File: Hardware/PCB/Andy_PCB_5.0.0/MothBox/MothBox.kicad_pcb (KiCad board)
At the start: 2 copper layers, 237 x 140.5 mm, 184 parts, among them P1 Raw Input, P2 12V Regulated Input, P3 Input to regulator, P4 External Attractor, Q1 BC817, Q10 BC817, Q11 BC817, Q2 TJ10S04M3L,LXHQ, Q4 BC817, Q5 TJ10S04M3L,LXHQ, Q6 BC817, Q7 TJ10S04M3L,LXHQ, Q8 BC817, Q9 BC817, U1 Days, U10 IRF9335TRPBF, U11 IRF9335TRPBF, U12 IRF9335TRPBF, U13 IRF9335TRPBF, U16 Female Inv Socket Pi 2.54-2*20, U18 RASPBERRY_PI_4B_4GB, U19 INA219BIDCNT, U2 Hours1, U3 XL4015E1, U5 RASPBERRY_PI_5, U6 Hours2, U7 Modes, U8 CD74HC4067M96E4, U9 CD74HC4067M96E4

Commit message: fillet lines
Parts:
- removed D1: S10MC, easyeda2kicad:SMC_L7.1-W6.2-LS8.1-RD
- added H9: GPS 4 pin 2.54-1*4P母, AQLibrary:GPS4pin_HDR-TH_4P-P2.54-V-F, F.Cu at (-46.5, 49.5)
- added U17: GPs 5 pin PM2.54-1*5, AQLibrary:GPS5pin_HDR-TH_5P-P2.54-V-F, F.Cu at (-18.6, 48.5)
- R64, R65: value 10K -> 4k7
- U5: footprint Connector_PinHeader_2.54mm:PinHeader_2x20_P2.54mm_Vertical -> AQLibrary:EPAPER_PinHeader_2x20_P2.54mm_Vertical
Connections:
- net /RPI5/STM_RX renamed GPS_TX
- net /RPI5/STM_TX renamed GPS_RX
- F2 pad 2: Net-(F2-Pad2) -> /Power/PWR_IN
- P1 pad 2: Net-(F2-Pad2) -> /Power/PWR_IN
- P2 pad 2: Net-(D1-A) -> +12V
- P3 pad 2: /Power/PWR_IN -> /Power/VIN-
- Q2 pad 3: /Power/PWR_IN -> /Power/VIN-
- R1 pad 2: /Power/PWR_IN -> /Power/VIN-
- R63 pad 1: /Power/PWR_IN -> /Power/VIN-
- U19 pad 2: /Power/PWR_IN -> /Power/VIN-
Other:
- outline, holes or cut-outs redrawn

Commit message: Tweaked Mothbeam and added GPS footprints
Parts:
- removed H4, H7: MountingHole_1/4inbolt, MountingHole:MountingHole_6.4mm_M6_Pad
- removed JP1: SolderJumper_2_Open, Jumper:SolderJumper-2_P1.3mm_Open_RoundedPad1.0x1.5mm
- A1, A2, A3: footprint Attractor:attractor -> Attractor:HDR-TH_4P-P2.54-H-M-W10.4
- E3: footprint SK54C:DIO_SK54C -> easyeda2kicad:SMC_L6.9-W5.9-LS8.0-RD
- H9, U17: moved to B.Cu
- P1, P2, P3, P4: footprint easyeda2kicad:CONN-TH_DB301V-3.5-2P-GN -> easyeda2kicad:CONN-TH_2P-P5.08_DIBO_DB142R-5.08-2P
- moved P4 160.3 mm to (102.5, 117.8), turned to -90 degrees
- moved R58 153.7 mm to (181.5, 81.8), turned to -90 degrees
- moved R55 141.7 mm to (178.5, 81.8)
- moved R48 128.4 mm to (191.2, 84.8)
- moved R47 128.4 mm to (193.5, 84.8)
- moved H9 121.1 mm to (53.2, 118.2), turned to -90 degrees
- moved R50 115.5 mm to (185.3, 81.8)
- moved R49 115.5 mm to (187.5, 81.8)
- moved U17 106.9 mm to (62.5, 118.2), turned to -90 degrees
- moved A1 99.1 mm to (196.5, 71.8), turned to -90 degrees
- moved U13 89.8 mm to (149.5, 89.8)
- moved L1 67.1 mm to (166.5, 105.8)
- moved U12 62.2 mm to (154.5, 75.8)
- moved A3 52.8 mm to (102.5, 71.8), turned to -90 degrees
- moved A2 31.9 mm to (249.5, 71.8), turned to -90 degrees
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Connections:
- net /Switches/Armed/Disarmed renamed /GPS and Switches/Armed/Disarmed
- net /Switches/Attractor_1 renamed /GPS and Switches/Attractor_1
- net /Switches/Attractor_2 renamed /GPS and Switches/Attractor_2
- net /Switches/Attractor_3 renamed /GPS and Switches/Attractor_3
- net /Switches/C1 renamed /GPS and Switches/C1
- net /Switches/C2 renamed /GPS and Switches/C2
- net /Switches/Fri renamed /GPS and Switches/Fri
- net /Switches/HI/LOW_PWR renamed /GPS and Switches/HI/LOW_PWR
- net /Switches/Hour_1 renamed /GPS and Switches/Hour_1
- net /Switches/Hour_10 renamed /GPS and Switches/Hour_10
- net /Switches/Hour_11 renamed /GPS and Switches/Hour_11
- net /Switches/Hour_12 renamed /GPS and Switches/Hour_12
- net /Switches/Hour_13 renamed /GPS and Switches/Hour_13
- net /Switches/Hour_14 renamed /GPS and Switches/Hour_14
- net /Switches/Hour_15 renamed /GPS and Switches/Hour_15
- net /Switches/Hour_16 renamed /GPS and Switches/Hour_16
- net /Switches/Hour_2 renamed /GPS and Switches/Hour_2
- net /Switches/Hour_3 renamed /GPS and Switches/Hour_3
- net /Switches/Hour_4 renamed /GPS and Switches/Hour_4
- net /Switches/Hour_5 renamed /GPS and Switches/Hour_5
- net /Switches/Hour_6 renamed /GPS and Switches/Hour_6
- net /Switches/Hour_7 renamed /GPS and Switches/Hour_7
- net /Switches/Hour_8 renamed /GPS and Switches/Hour_8
- net /Switches/Hour_9 renamed /GPS and Switches/Hour_9
- net /Switches/INT/EXT_Attractor renamed /GPS and Switches/INT/EXT_Attractor
- net /Switches/Mon renamed /GPS and Switches/Mon
- net /Switches/Sat renamed /GPS and Switches/Sat
- net /Switches/Sun renamed /GPS and Switches/Sun
- net /Switches/Test_Debug renamed /GPS and Switches/Test_Debug
- net /Switches/Thur renamed /GPS and Switches/Thur
- net /Switches/Tue renamed /GPS and Switches/Tue
- net /Switches/Wed renamed /GPS and Switches/Wed
- A1 pad 1: unconnected-(A1-EN-Pad1) -> /UV LED PCB/+12V_PCB2
- A1 pad 2: unconnected-(A1-EN-Pad2) -> /UV LED PCB/+12V_PCB2
- A1 pad 3: /UV LED PCB/+12V_PCB2 -> GND
- A1 pad 4: /UV LED PCB/+12V_PCB2 -> GND
- A2 pad 1: unconnected-(A2-EN-Pad1) -> /UV LED PCB/+12V_PCB1
- A2 pad 2: unconnected-(A2-EN-Pad2) -> /UV LED PCB/+12V_PCB1
- A2 pad 3: /UV LED PCB/+12V_PCB1 -> GND
- A2 pad 4: /UV LED PCB/+12V_PCB1 -> GND
- A3 pad 1: unconnected-(A3-EN-Pad1) -> /UV LED PCB/+12V_PCB3
- A3 pad 2: unconnected-(A3-EN-Pad2) -> /UV LED PCB/+12V_PCB3
- A3 pad 3: /UV LED PCB/+12V_PCB3 -> GND
- A3 pad 4: /UV LED PCB/+12V_PCB3 -> GND
- L1 pad 1: Net-(E3-PadC) -> Net-(E3-C)
- U16 pad 30: EN_MUX2 -> EN_MUX1
- U16 pad 31: /RPI5/TimeP -> GPS_PPS
- U16 pad 32: L_LED_CTRL -> EN_MUX2
- U16 pad 36: RPI_CTRL -> L_LED_CTRL
- U3 pad 3: Net-(E3-PadC) -> Net-(E3-C)
- U5 pad 29: EN_MUX2 -> EN_MUX1
- U5 pad 31: L_LED_CTRL -> EN_MUX2
- U5 pad 32: /RPI5/TimeP -> GPS_PPS
- U5 pad 35: RPI_CTRL -> L_LED_CTRL
- U8 pad 15: GND -> EN_MUX1
- U9 pad 15: GND -> EN_MUX2
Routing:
- net GND: vias 143 -> 131
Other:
- board text added: "+ -"
- board text added: "Regulator Input"
- board text removed: "DAYS"
- board text removed: "HI UV INT LO FUL EX"
- board text removed: "LED LEVEL"
- board text removed: "to Regulator"

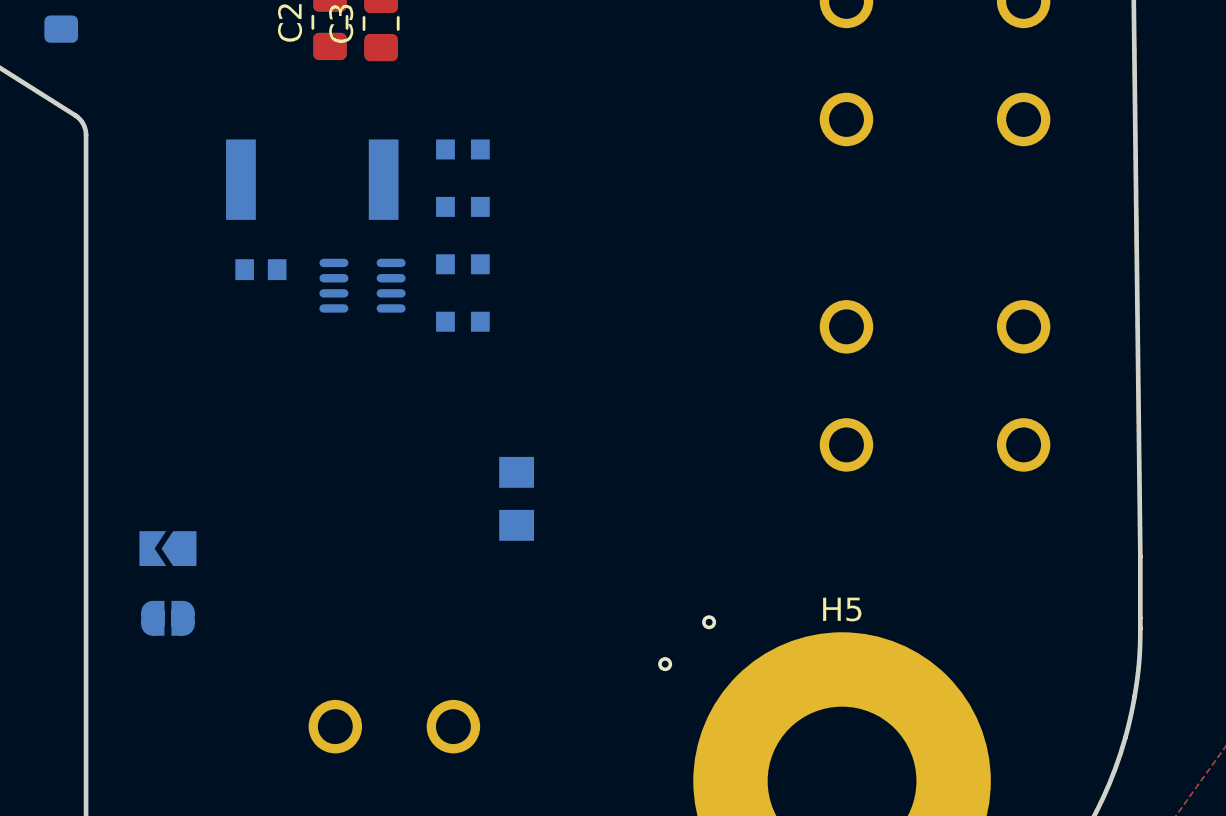
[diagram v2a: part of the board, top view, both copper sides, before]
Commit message: started adding test points, fixed current sensor should be 3.3v
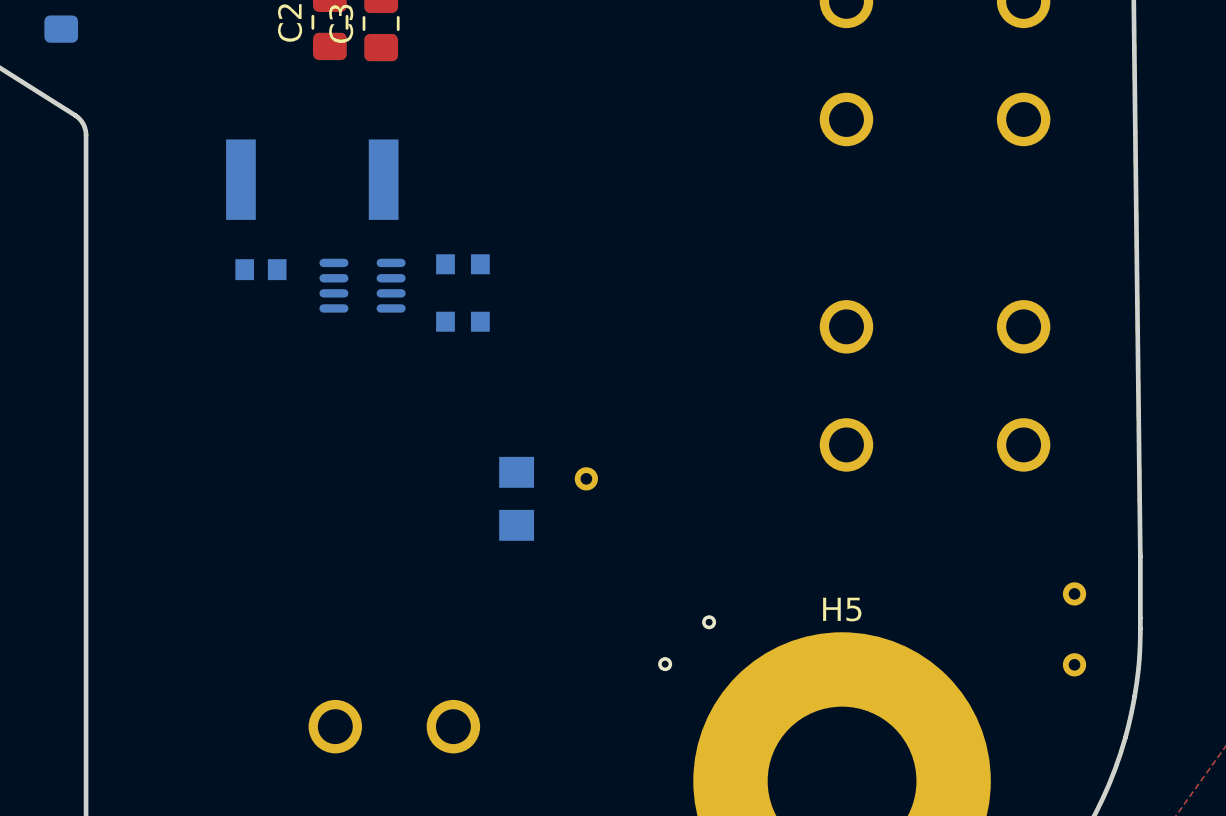
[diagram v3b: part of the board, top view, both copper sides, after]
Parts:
- removed R61, R62: 10K, easyeda2kicad:R0603
- removed SJ1: SOLDERJUMPERREFLOW_NOPASTE, Jumper:SolderJumper-2_P1.3mm_Open_RoundedPad1.0x1.5mm
- removed SJ2: SOLDERJUMPERREFLOW_NOPASTE, Jumper:SolderJumper-2_P1.3mm_Open_TrianglePad1.0x1.5mm
- added TP1: TestPoint, TestPoint:TestPoint_THTPad_D1.0mm_Drill0.5mm, B.Cu at (265.5, 184.7)
- added TP2: TestPoint, TestPoint:TestPoint_THTPad_D1.0mm_Drill0.5mm, B.Cu at (265.5, 187.8)
- added TP3: TestPoint, TestPoint:TestPoint_THTPad_D1.0mm_Drill0.5mm, B.Cu at (244.5, 179.8)
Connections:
- C6 pad 2: +5V -> +3.3V
- R64 pad 2: +5V -> +3.3V
- R65 pad 2: +5V -> +3.3V
- U19 pad 4: +5V -> +3.3V

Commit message: before i kill the pullup resistors
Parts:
- removed R21, R23, R25, R26, R39, R42, R43, R44: DNP, Resistor_SMD:R_0805_2012Metric
- added TP4: VIN_-, TestPoint:TestPoint_THTPad_D1.0mm_Drill0.5mm, B.Cu at (247.5, 175.8)
- C2, C3, R4, R45, R46, R5, R56, R58, R59: moved to B.Cu
- Q10, R2, R3, R79, R81, U10: moved to F.Cu
- R64, R65: value 4k7 -> 10k
- TP1: value TestPoint -> A0_meas
- TP2: value TestPoint -> A1_meas
- TP3: value TestPoint -> 5V_test
- moved R38 382.3 mm to (354.6, 74.3), turned to 90 degrees
- moved R37 377.8 mm to (349.6, 74.3), turned to 90 degrees
- moved R36 373.3 mm to (344.6, 74.3), turned to 90 degrees
- moved R41 362.8 mm to (332.5, 74.3), turned to 90 degrees
- moved R40 358.6 mm to (327.4, 74.3), turned to 90 degrees
- moved R35 352.4 mm to (319.9, 74.3), turned to 90 degrees
- moved R34 348.6 mm to (315.0, 74.3), turned to 90 degrees
- moved R56 341.6 mm to (311.9, 74.3), turned to 90 degrees
- moved R45 297.6 mm to (311.0, 89.8), turned to -90 degrees
- moved R46 294.0 mm to (308.0, 89.8), turned to -90 degrees
- moved R59 209.9 mm to (293.0, 89.8), turned to -90 degrees
- moved R2 184.5 mm to (98.0, 154.8), turned to 0 degrees
- moved R3 176.6 mm to (106.0, 161.3), turned to 0 degrees
- moved R57 149.9 mm to (304.5, 46.8)
- moved U10 129.6 mm to (293.5, 46.3), turned to 0 degrees
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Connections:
- P3 pad 2: /Power/VIN- -> Net-(Q2-D)
- TP3 pad 1: /Power/VIN+ -> +5V
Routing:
- net +3.3V: track 29.0 -> 0.00 mm
- net Net-(Q11-C): track 2.62 -> 0.00 mm
- net +5V: track 0.00 -> 2.54 mm
- net GND: track 2.53 -> 0.00 mm, vias 131 -> 0
- net Net-(Q11-B): track 2.28 -> 0.00 mm
- net Net-(Q9-B): track 2.24 -> 0.00 mm
- net /Power/FB: track 2.15 -> 0.00 mm

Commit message: Groups photos leds, started routing
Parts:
- removed R16, R17, R18, R19, R20, R22, R24, R27, R28, R29, R30, R31, R32, R33, R34, R35, R36, R37, R38, R40, R41, R45, R46, R47, R48, R49, R50, R56, R58, R59, R60: 10k, Resistor_SMD:R_0805_2012Metric
- C17: moved to B.Cu
- D30, D31, Q11, Q8, Q9, R75, R76, R77, R78, R80, R82, U11, U12: moved to F.Cu
- moved R52 547.7 mm to (-208.1, 247.1)
- moved Q7 485.4 mm to (-136.2, 242.8)
- moved R51 445.3 mm to (-313.5, 135.3), turned to 0 degrees
- moved LED20 437.4 mm to (-362.5, 248.2), turned to 180 degrees
- moved LED22 437.2 mm to (-362.5, 255.3), turned to 180 degrees
- moved LED21 436.8 mm to (-362.0, 251.8)
- moved Q5 433.4 mm to (-122.7, 101.8)
- moved R57 433.4 mm to (-123.6, 114.0)
- moved LED25 428.6 mm to (-344.0, 255.3), turned to 180 degrees
- moved R69 421.5 mm to (-129.7, 271.3)
- moved LED24 421.1 mm to (-348.5, 249.8), turned to 90 degrees
- moved LED23 417.0 mm to (-344.5, 244.8)
- moved R66 407.8 mm to (-171.7, 252.8), turned to -90 degrees
- moved LED26 400.0 mm to (-318.0, 244.2)
- moved LED27 400.0 mm to (-318.0, 248.2)
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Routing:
- net /RPI5/GPIO4/GPIO_GCKL: track 0.00 -> 245.4 mm
- net SDA: track 0.00 -> 236.8 mm
- net /RPI5/Save for eink_11: track 0.00 -> 235.4 mm
- net SCL: track 0.00 -> 234.6 mm
- net /RPI5/Save for eink_22: track 0.00 -> 215.6 mm
- net /RPI5/Save for eink_24: track 0.00 -> 209.0 mm
- net /RPI5/Save for eink_19: track 0.00 -> 188.2 mm
- net /RPI5/Save for eink_23: track 0.00 -> 181.0 mm
- net /RPI5/ID_SD: track 0.00 -> 173.8 mm
- net /RPI5/Save for relay: track 0.00 -> 172.8 mm
- net /RPI5/Save for relay 2: track 0.00 -> 164.1 mm
- net L_LED_CTRL: track 0.00 -> 164.0 mm
- net /RPI5/Save for relay 3: track 0.00 -> 161.6 mm
- net GPS_TX: track 0.00 -> 60.3 mm
- net +3.3V: track 0.00 -> 37.6 mm
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- removed copper zone on B.Cu, net +12V

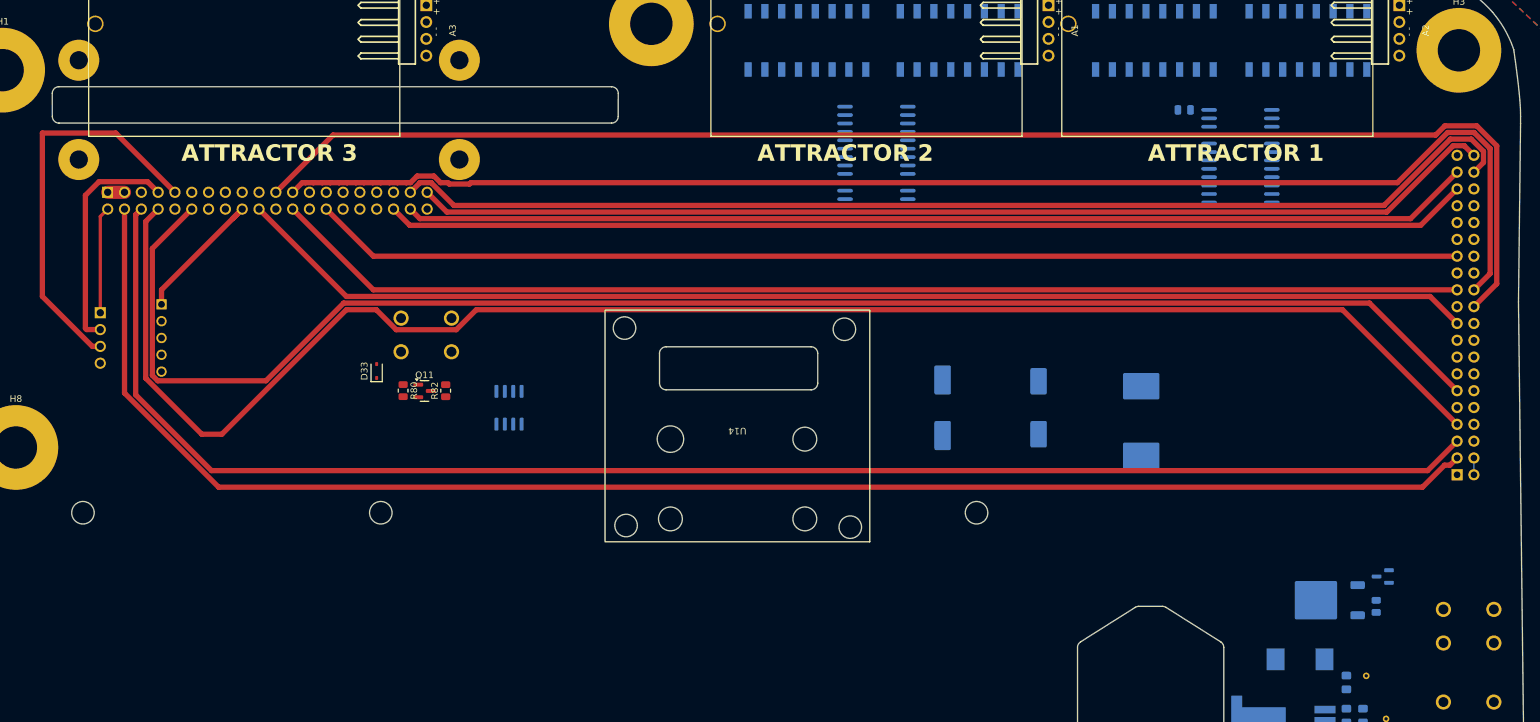
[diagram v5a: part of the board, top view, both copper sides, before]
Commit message: Moved Epaper and routed epaper and relay wires
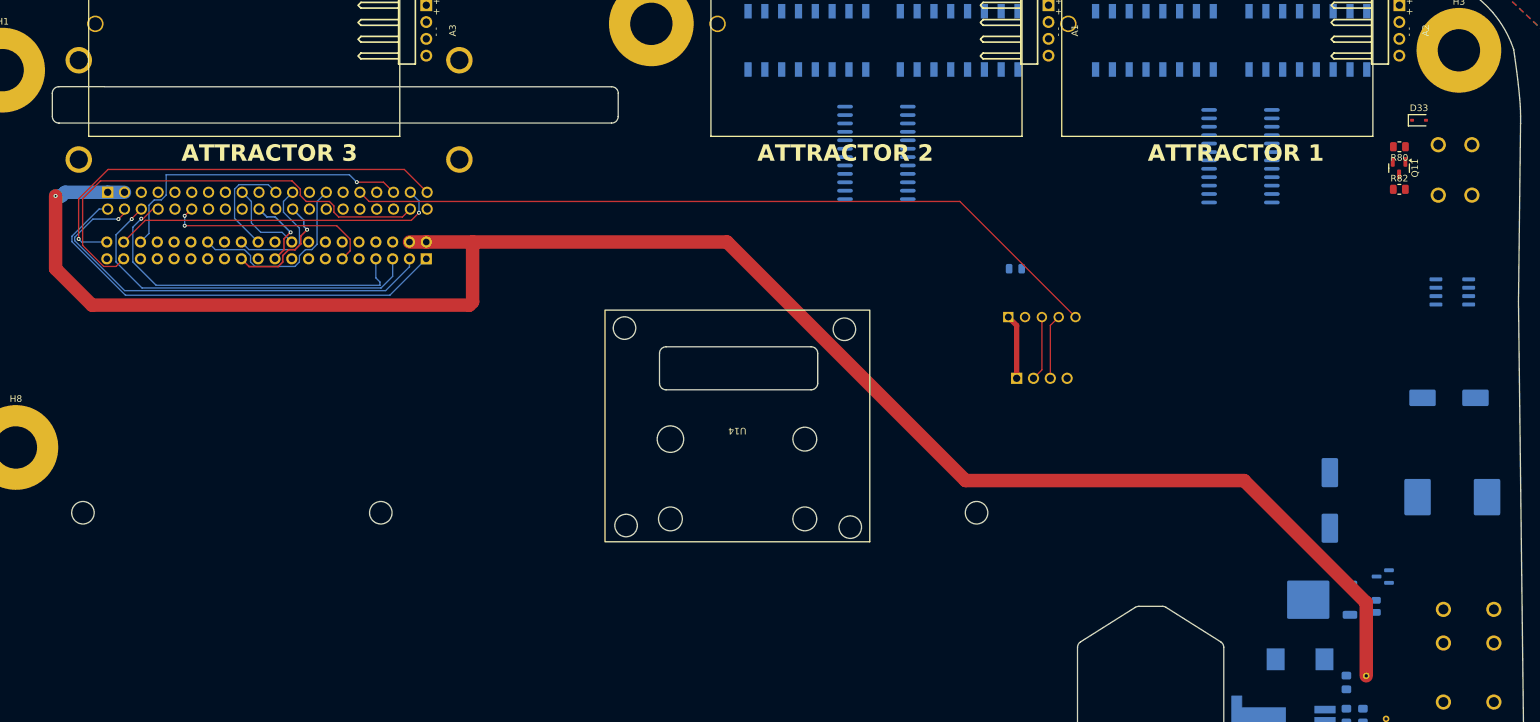
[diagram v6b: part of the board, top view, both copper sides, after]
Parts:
- moved D33 162.0 mm to (252.5, 85.3), turned to 0 degrees
- moved U5 159.1 mm to (102.5, 106.3), turned to 90 degrees
- moved P4 157.4 mm to (257.9, 92.8), turned to 180 degrees
- moved R80 155.0 mm to (249.5, 89.3), turned to 180 degrees
- moved Q11 151.0 mm to (249.5, 92.6), turned to -90 degrees
- moved R82 147.2 mm to (249.5, 95.8), turned to 0 degrees
- moved U13 143.6 mm to (257.5, 111.3), turned to 180 degrees
- moved H9 142.4 mm to (195.5, 124.3), turned to 0 degrees
- moved U17 133.0 mm to (195.5, 115.1), turned to 0 degrees
- moved C4 62.0 mm to (257.0, 127.3), turned to 180 degrees
- moved C1 60.2 mm to (239.0, 142.8)
- moved L1 48.4 mm to (257.5, 142.3), turned to 0 degrees
- moved C17 35.0 mm to (191.5, 107.8), turned to 180 degrees
- moved Q2 1.16 mm to (237.0, 157.8)
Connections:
- U16 pad 18: +3.3V -> unconnected-(U16-Pad18)
- U16 pad 27: /RPI5/ID_SC -> unconnected-(U16-Pad27)
- U16 pad 28: /RPI5/ID_SD -> unconnected-(U16-Pad28)
- U5 pad 17: +3.3V -> unconnected-(U5-3V3-Pad17)
- U5 pad 27: /RPI5/ID_SD -> unconnected-(U5-ID_SD-Pad27)
- U5 pad 28: /RPI5/ID_SC -> unconnected-(U5-ID_SC-Pad28)
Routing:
- net +5V: track 5.08 -> 274.3 mm, vias 0 -> 1
- net /RPI5/Save for eink_11: track 235.4 -> 32.3 mm, vias 0 -> 2
- net /RPI5/Save for eink_22: track 215.6 -> 16.5 mm
- net /RPI5/GPIO4/GPIO_GCKL: track 245.4 -> 53.3 mm, vias 0 -> 1
- net /RPI5/Save for eink_24: track 209.0 -> 19.1 mm
- net SCL: track 234.6 -> 56.4 mm, vias 0 -> 1
- net /RPI5/Save for eink_19: track 188.2 -> 11.2 mm, vias 0 -> 1
- net /RPI5/ID_SD: track 173.8 -> 0.00 mm
- net SDA: track 236.8 -> 66.6 mm, vias 0 -> 1
- net L_LED_CTRL: track 164.0 -> 0.00 mm
- net /RPI5/Save for eink_23: track 181.0 -> 18.0 mm, vias 0 -> 1
- net /RPI5/Save for relay: track 172.8 -> 50.1 mm, vias 0 -> 1
- net GPS_PPS: track 0.00 -> 115.9 mm
- net /RPI5/Save for relay 2: track 164.1 -> 66.4 mm, vias 0 -> 1
- net /RPI5/Save for relay 3: track 161.6 -> 69.5 mm
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
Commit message: Almost all powr is wiered
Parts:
- moved C1 38.8 mm to (259.5, 175.8)
- moved L1 35.7 mm to (222.5, 149.3), turned to 90 degrees
- moved C4 34.9 mm to (222.5, 132.3), turned to 90 degrees
- moved P2 19.5 mm to (259.5, 142.3)
- moved P3 19.5 mm to (259.5, 156.3)
- moved C2 5.14 mm to (245.5, 199.8), turned to -90 degrees
- moved Q1 4.61 mm to (246.0, 149.8), turned to -90 degrees
- moved D33 4.03 mm to (256.5, 85.3)
- moved H5 2.55 mm to (258.0, 192.3)
- moved R82 1.00 mm to (249.5, 96.8), turned to -90 degrees
- moved TP2 1.00 mm to (248.5, 198.8)
- moved C17 0.50 mm to (191.5, 108.3)
- turned U13 to 0 degrees
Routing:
- net EN_12VReg: track 0.00 -> 243.2 mm
- net +3.3V: track 76.9 -> 270.1 mm
- net +12V: track 0.00 -> 72.4 mm
- net /Power/PWR_IN: track 0.00 -> 56.3 mm, vias 0 -> 1
- net COM_I/O: track 47.8 -> 0.00 mm, vias 1 -> 0
- net Net-(E3-C): track 0.00 -> 32.0 mm
- net /Power/VIN-: track 0.00 -> 31.2 mm
- net /UV LED PCB/+12V_PCB4: track 0.00 -> 22.2 mm
- net +5V: track 274.3 -> 292.8 mm, vias 1 -> 2
- net Net-(Q1-C): track 0.00 -> 17.4 mm, vias 0 -> 2
- net Net-(U19-A0): track 0.00 -> 17.3 mm
- net Net-(Q11-C): track 0.00 -> 17.0 mm, vias 0 -> 1
- net Net-(Q2-D): track 0.00 -> 14.3 mm
- net Net-(U19-A1): track 0.00 -> 13.6 mm
- net GND: track 0.00 -> 7.62 mm
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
